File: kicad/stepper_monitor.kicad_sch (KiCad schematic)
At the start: 63 parts, among them J1 Conn_01x04_Pin, J2 Conn_01x04_Pin, J3 Conn_01x02_Pin, J4 USB_C_Receptacle_USB2.0, J5 JTAG, M1 Motor-simple_stepper_motor_an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, Q1 MMDT2222A, SW1 SW_Push, U1 5V, U2 CP2102N-A01-GQFN28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

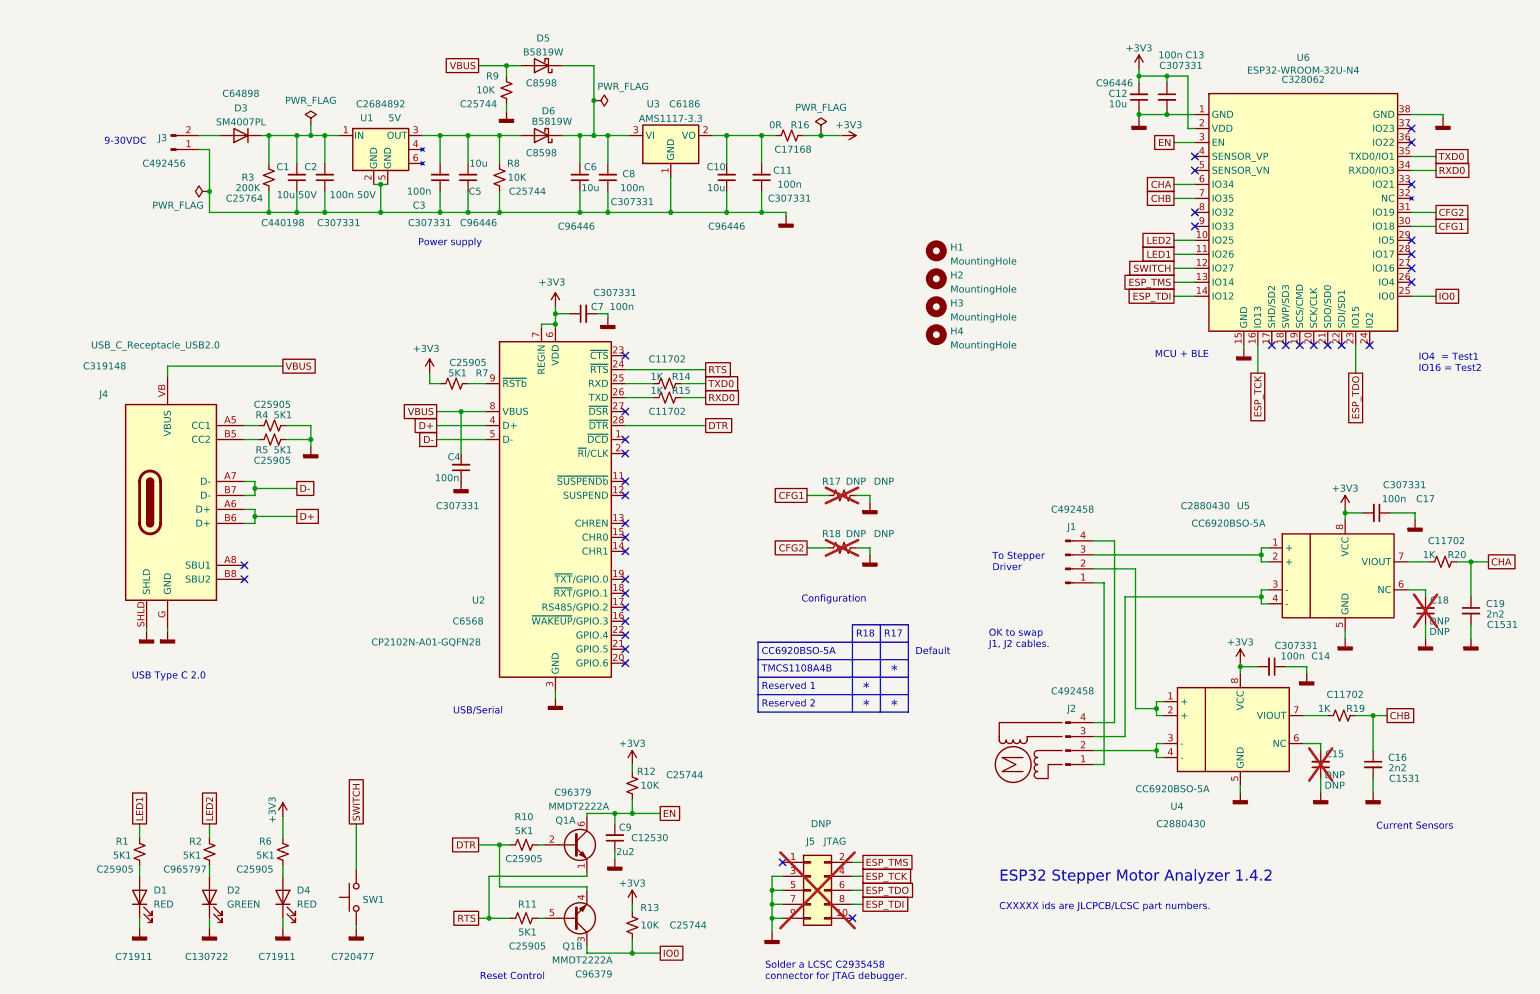
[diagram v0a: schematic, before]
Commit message: New version without Mornsun regulator
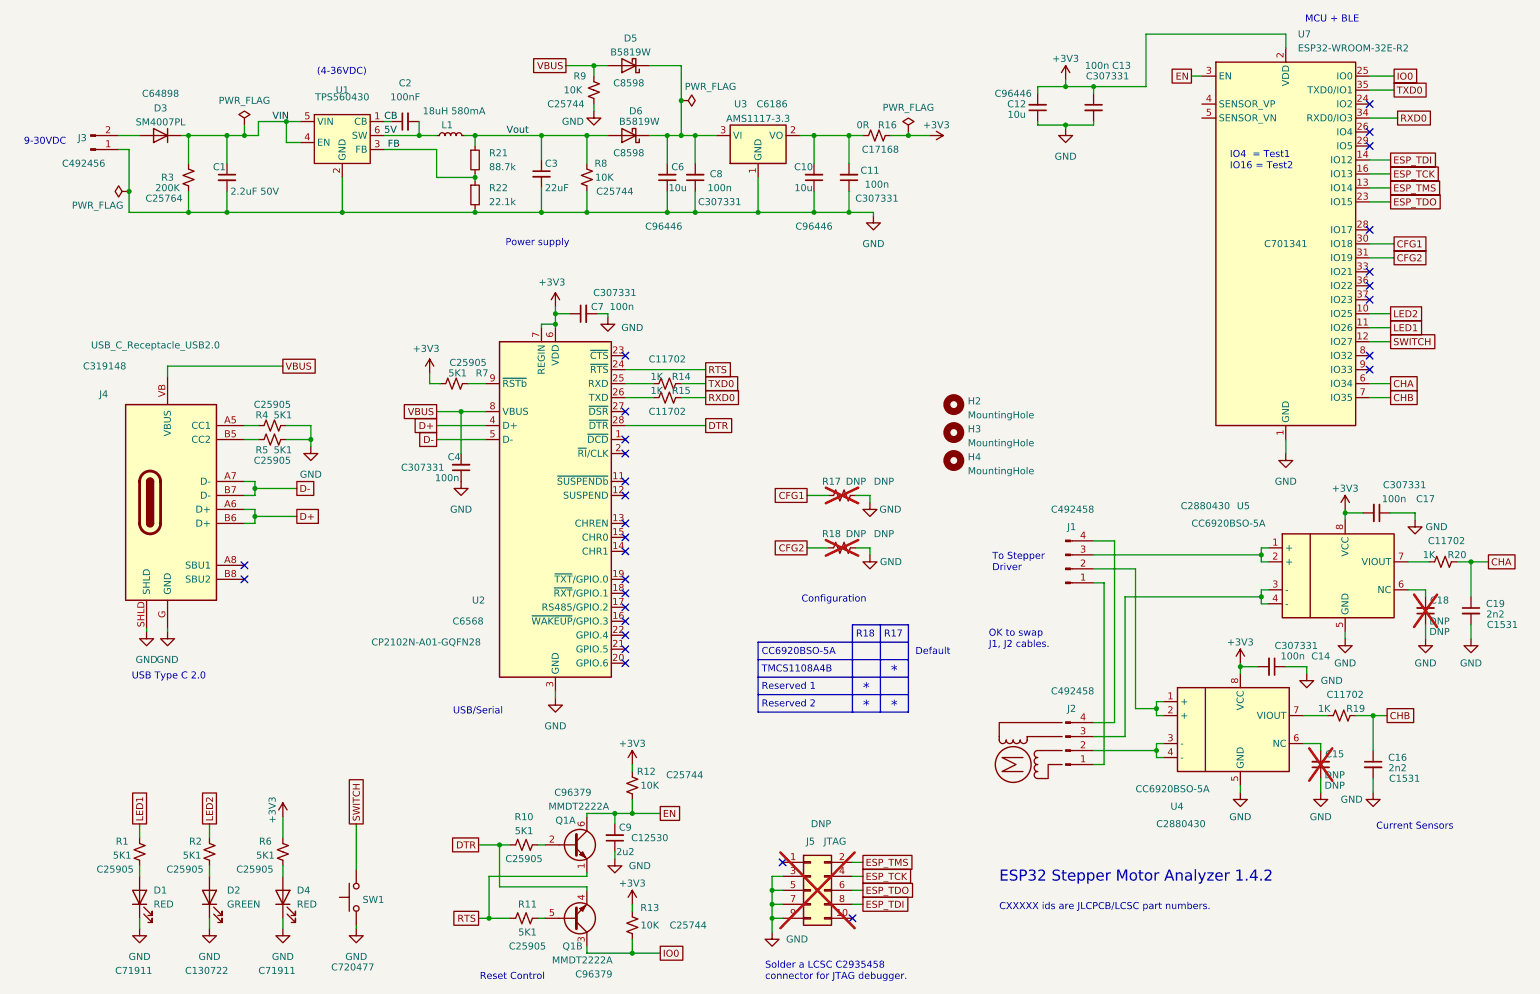
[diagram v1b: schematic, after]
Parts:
- removed C5: 10u, Capacitor_SMD:C_0603_1608Metric, symbol Device:C_Small
- removed H1: MountingHole, MountingHole:MountingHole_3.2mm_M3_Pad_Via, symbol Mechanical:MountingHole
- removed U1: 5V, stepper_monitor:Converter_DCDC, symbol stepper_monitor:DC_DC
- removed U6: ESP32-WROOM-32U-N4, stepper_monitor:ESP32-WROOM-32U, symbol stepper_monitor:ESP32-WROOM-32D
- added L1: 18uH 580mA, Inductor_SMD:L_Sunlord_SWPA3012S, symbol Device:L_Small
- added R21: 88.7k, Resistor_SMD:R_0603_1608Metric, symbol Device:R_Small
- added R22: 22.1k, Resistor_SMD:R_0603_1608Metric, symbol Device:R_Small
- added U1: TPS560430, Package_TO_SOT_SMD:SOT-23-6, symbol stepper_monitor:TPS560430XDBVR
- added U7: ESP32-WROOM-32E-R2, RF_Module:ESP32-WROOM-32D, symbol RF_Module:ESP32-WROOM-32E-R2
- C1: value 10u 50V -> 2.2uF 50V; footprint Capacitor_SMD:C_0805_2012Metric -> Capacitor_SMD:C_0603_1608Metric; LCSC C440198 -> C913904
- C15, C18, H2, H3, H4, J5, R17, R18: now left out of the parts list
- C2: value 100n 50V -> 100nF; LCSC C307331 -> C1525
- C3: value 100n -> 22uF; footprint Capacitor_SMD:C_0402_1005Metric -> Capacitor_SMD:C_0603_1608Metric; LCSC C307331 -> C86295
- D5, D6: value B5819W -> B5819W
- R2: LCSC C965797 -> C25905
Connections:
- net +3V3: now also U7.2 (VDD)
- net CFG1: now also U7.30 (IO18)
- net CFG2: now also U7.31 (IO19)
- net CHA: now also U7.6 (IO34)
- net CHB: now also U7.7 (IO35)
- net EN: now also U7.3 (EN)
- net ESP_TCK: now also U7.16 (IO13)
- net ESP_TDI: now also U7.14 (IO12)
- net ESP_TDO: now also U7.23 (IO15)
- net ESP_TMS: now also U7.13 (IO14)
- net IO0: now also U7.25 (IO0)
- net LED1: now also U7.11 (IO26)
- net LED2: now also U7.10 (IO25)
- net RXD0: now also U7.34 (RXD0/IO3)
- net SWITCH: now also U7.12 (IO27)
- net TXD0: now also U7.35 (TXD0/IO1)
- net VIN: now reaches D3.1 (K), R3.1
- net VIN: now also C1.1, U1.4 (EN), U1.5 (VIN); no longer C1.2, C2.2
- net Vout: now reaches D6.2 (A), R8.2
- net Vout: now also C3.1, L1.2, R21.1; no longer C3.2
- net GNDD renamed GND
- net GND: now also C1.2, C3.2, R22.2, U1.2 (GND), U7.1 (GND), U7.15 (GND), U7.38 (GND), U7.39 (GND); no longer C1.1, C2.1, C3.1
- new net 5V: C2.2, L1.1, U1.6 (SW)
- new net CB: C2.1, U1.1 (CB)
- new net FB: R21.2, R22.1, U1.3 (FB)
- no-connect marks 38 -> 29
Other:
- note added: "(4-36VDC)"
- moved on the sheet: C10, C11, C6, C8, D3, D5, D6, H4, J3, R16, R3, R8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
